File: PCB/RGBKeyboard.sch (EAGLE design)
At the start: 50 parts, among them U1 3341, U10 3341, U11 3341, U12 3341, U13 3341, U14 3341, U2 3341, U3 3341, U4 3341, U5 3341, U6 3341, U7 3341, U8 3341, U9 3341

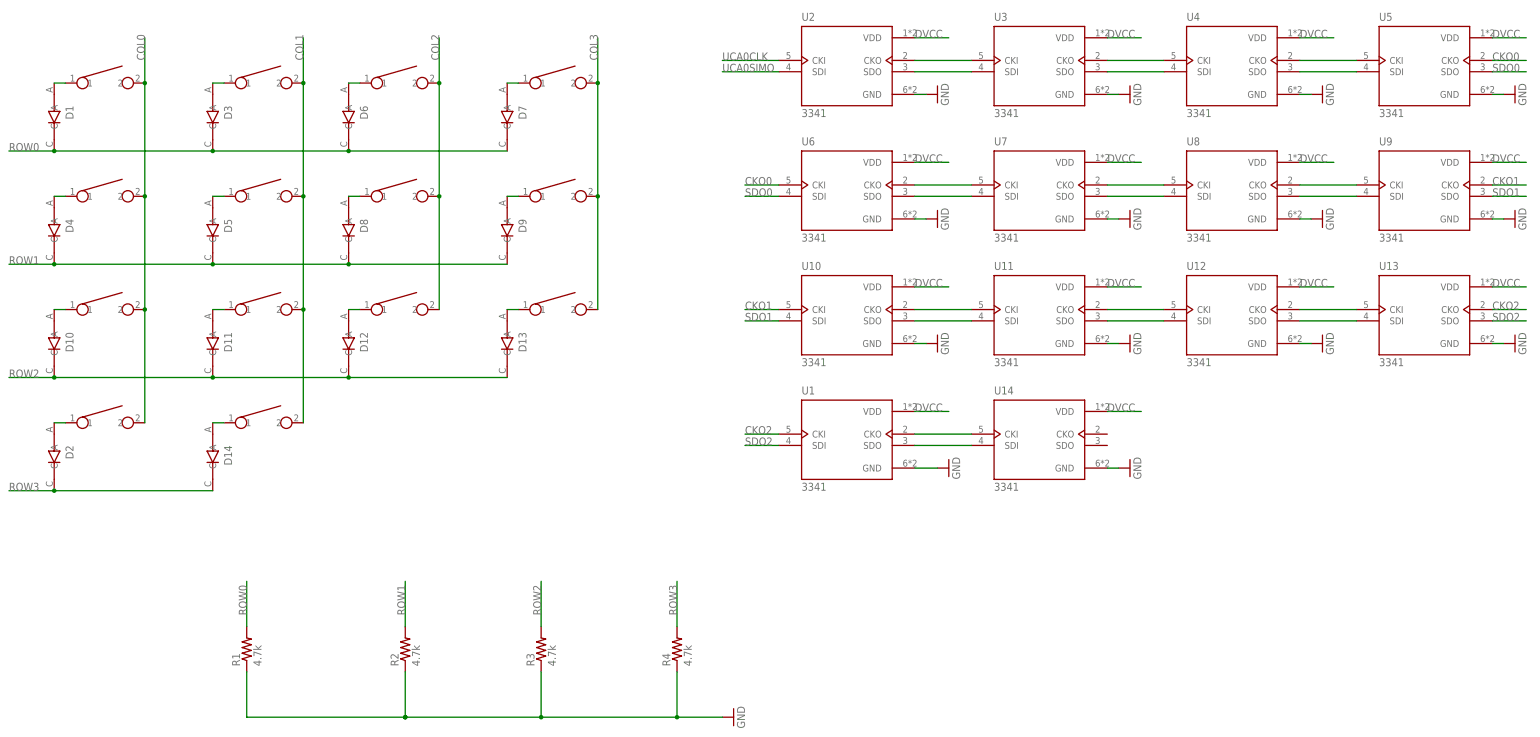
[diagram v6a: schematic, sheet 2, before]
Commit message: Schematic and Board for first prototype
Ended up removing the LEDs entirely (rip) because
there was too much uncertainty with dimensions
and routing was annoying
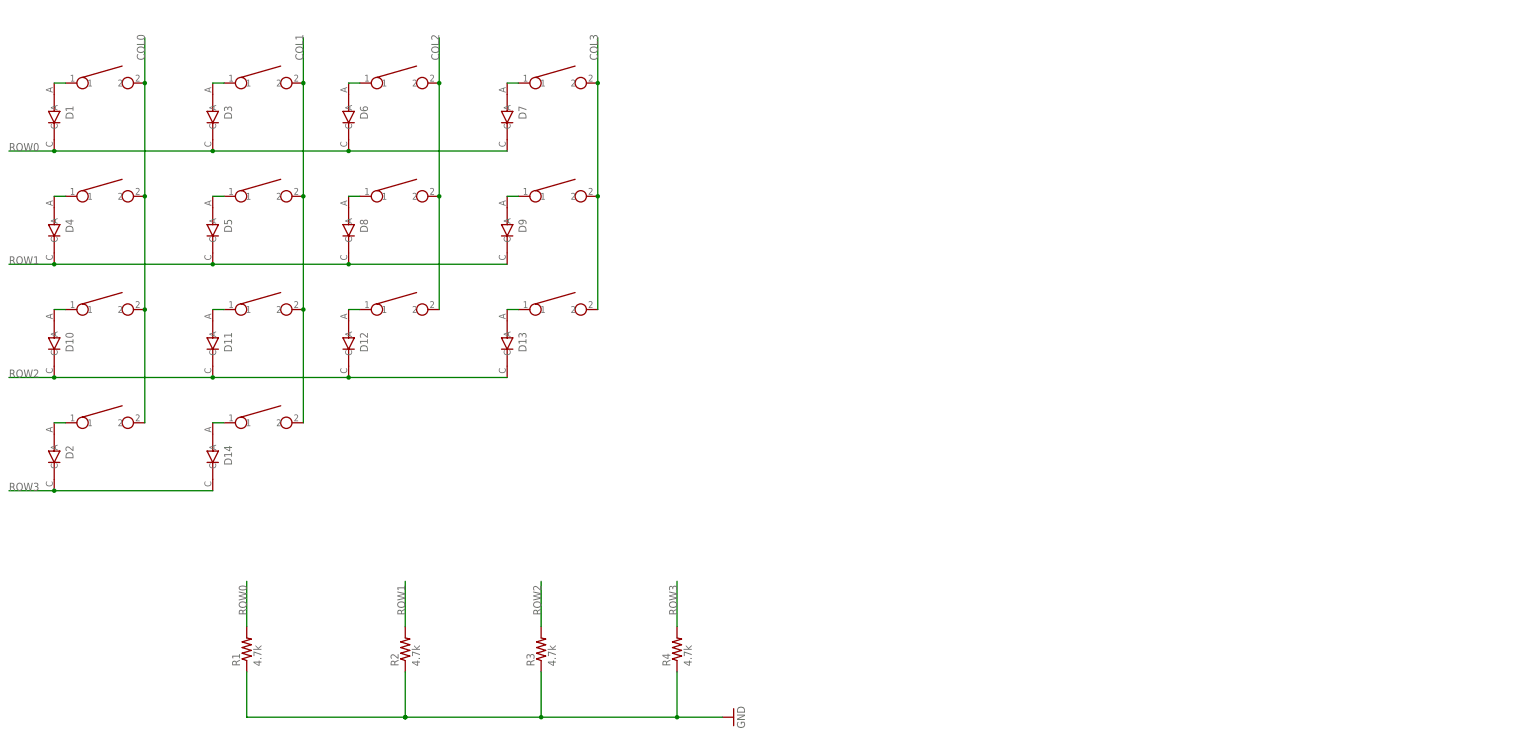
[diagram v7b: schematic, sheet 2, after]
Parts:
- removed SV5: (no value), con-lstb:MA03-1
- removed U1, U10, U11, U12, U13, U14, U2, U3, U4, U5, U6, U7, U8, U9: 3341, 3341:3341
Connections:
- removed net CKO0: U5.CKO, U6.CKI
- removed net CKO1: U10.CKI, U9.CKO
- removed net CKO2: U1.CKI, U13.CKO
- removed net N$10: U1.SDO, U14.SDI
- removed net N$13: U2.CKO, U3.CKI
- removed net N$14: U2.SDO, U3.SDI
- removed net N$15: U3.CKO, U4.CKI
- removed net N$16: U3.SDO, U4.SDI
- removed net N$17: U4.CKO, U5.CKI
- removed net N$18: U4.SDO, U5.SDI
- removed net N$19: U6.CKO, U7.CKI
- removed net N$20: U6.SDO, U7.SDI
- removed net N$21: U7.CKO, U8.CKI
- removed net N$22: U7.SDO, U8.SDI
- removed net N$23: U8.CKO, U9.CKI
- removed net N$24: U8.SDO, U9.SDI
- removed net N$25: U10.CKO, U11.CKI
- removed net N$26: U10.SDO, U11.SDI
- removed net N$27: U11.CKO, U12.CKI
- removed net N$28: U11.SDO, U12.SDI
- removed net N$29: U12.CKO, U13.CKI
- removed net N$30: U12.SDO, U13.SDI
- removed net N$9: U1.CKO, U14.CKI
- removed net SDO0: U5.SDO, U6.SDI
- removed net SDO1: U10.SDI, U9.SDO
- removed net SDO2: U1.SDI, U13.SDO
- removed net UCA0CLK: SV5.3, U2.CKI
- removed net UCA0SIMO: SV5.2, U2.SDI
- net DVCC: no longer U1.VDD, U10.VDD, U11.VDD, U12.VDD, U13.VDD, U14.VDD, U2.VDD, U3.VDD, U4.VDD, U5.VDD, U6.VDD, U7.VDD, U8.VDD, U9.VDD
- net GND: no longer U1.GND, U10.GND, U11.GND, U12.GND, U13.GND, U14.GND, U2.GND, U3.GND, U4.GND, U5.GND, U6.GND, U7.GND, U8.GND, U9.GND

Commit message: New board design for 16 percent
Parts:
- removed D14, D2: BAV21W-7-F, BAV21W-7-F:BAV21W-7-F
- removed R1, R2, R3, R4: 4.7k, rcl:R-US_R0603
- removed SV1, SV3: (no value), con-lstb:MA04-1
- removed SV4: (no value), con-lstb:MA03-1
- added C1, C2, C3, C4: .1uF, rcl:C-USC0805
- added C5, C6: 4.7uF, rcl:C-USC0805
- added C7, C8: 22pF, rcl:C-USC0805
- added D16, D17, D18, D19: BAV21W-7-F, BAV21W-7-F:BAV21W-7-F
- added J1: UX60SC-MB-5S8, UX60SC-MB-5S8:UX60SC-MB-5S8
- added R5, R6: 10k, rcl:R-US_R0805
- added R7, R8: 22, rcl:R-US_R0805
- added SW1: TL3342F160QG/TR, TL3342F160QG_TR:TL3342F160QG/TR
- added U$15: CHERRY_MXCHERRY_MX_1_2, CHERRY_MX:CHERRY_MXCHERRY_MX_1_2
- added U$16, U$17, U$18, U$19: CHERRY_MX, CHERRY_MX:CHERRY_MX
- added U1: ATMEGA32U4-AUR, ATMEGA32U4-AUR:ATMEGA32U4-AUR
- added X1: FA-238, FA-238:FA-238
- U$14: value CHERRY_MXCHERRY_MX_1_6 -> CHERRY_MXCHERRY_MX_1_2; device CHERRY_MX:CHERRY_MXCHERRY_MX_1_6 -> CHERRY_MX:CHERRY_MXCHERRY_MX_1_2
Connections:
- removed net COL2: SV3.2, U$7.2, U$8.2, U$9.2
- removed net DVCC: SV4.3
- removed net N$4: D2.A, U$13.1
- removed net N$5: D14.A, U$14.1
- new net N$10: R6.2, U1.PE2(!HWB!)
- new net N$13: J1.VBUS, U1.UVCC
- new net N$14: R7.2, U1.D-
- new net N$15: J1.D-, R7.1
- new net N$16: R8.2, U1.D+
- new net N$17: J1.D+, R8.1
- new net N$18: D17.A, U$14.1, U$18.1
- new net N$19: D19.A, U$16.1
- new net N$20: D16.A, U$13.1, U$17.1
- new net N$21: D18.A, U$15.1, U$19.1
- new net N$22: U$10.2, U$11.2, U$12.2, U$16.2
- new net N$7: C8.2, U1.XTAL1, X1.3
- new net N$8: C7.2, U1.XTAL2, X1.1
- new net N$9: R5.1, SW1.1, SW1.2, U1.!RESET
- new net UCAP: C6.2, U1.UCAP
- new net VCC: C1.1, C2.1, C3.1, C4.1, C5.1, R5.2, U1.AVCC, U1.VBUS, U1.VCC
- net COL0: now also U$17.2; no longer SV3.4
- net COL1: now also U$18.2; no longer SV3.3
- net COL3: now also U$15.2, U$19.2, U$7.2, U$8.2, U$9.2; no longer SV3.1, U$10.2, U$11.2, U$12.2
- net GND: now also C1.2, C2.2, C3.2, C4.2, C5.2, C6.1, C7.1, C8.1, J1.GND, J1.SHIELD, R6.1, SW1.3, SW1.4, U1.GND, U1.UGND, X1.GND2, X1.GND4; no longer R1.1, R2.1, R3.1, R4.1, SV4.2
- net ROW0: no longer R1.2, SV1.4
- net ROW1: no longer R2.2, SV1.3
- net ROW2: no longer R3.2, SV1.2
- net ROW3: now also D16.C, D17.C, D18.C, D19.C; no longer D14.C, D2.C, R4.2, SV1.1
